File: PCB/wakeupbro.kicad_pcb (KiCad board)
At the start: 2 copper layers, 88.3 x 48.4 mm, 14 parts, among them J1 Conn_01x08_Pin, SW1 SW_Push, SW2 SW_Push, SW3 SW_Push, U1 XIAO-ESP32-C3-SMD

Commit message: Add finished PCB and exported step file of the PCB
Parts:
- added G***: LOGO, LOGO, F.Cu at (110.5, 49.6)
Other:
- board size 88.3 x 48.4 mm -> 90 x 50 mm

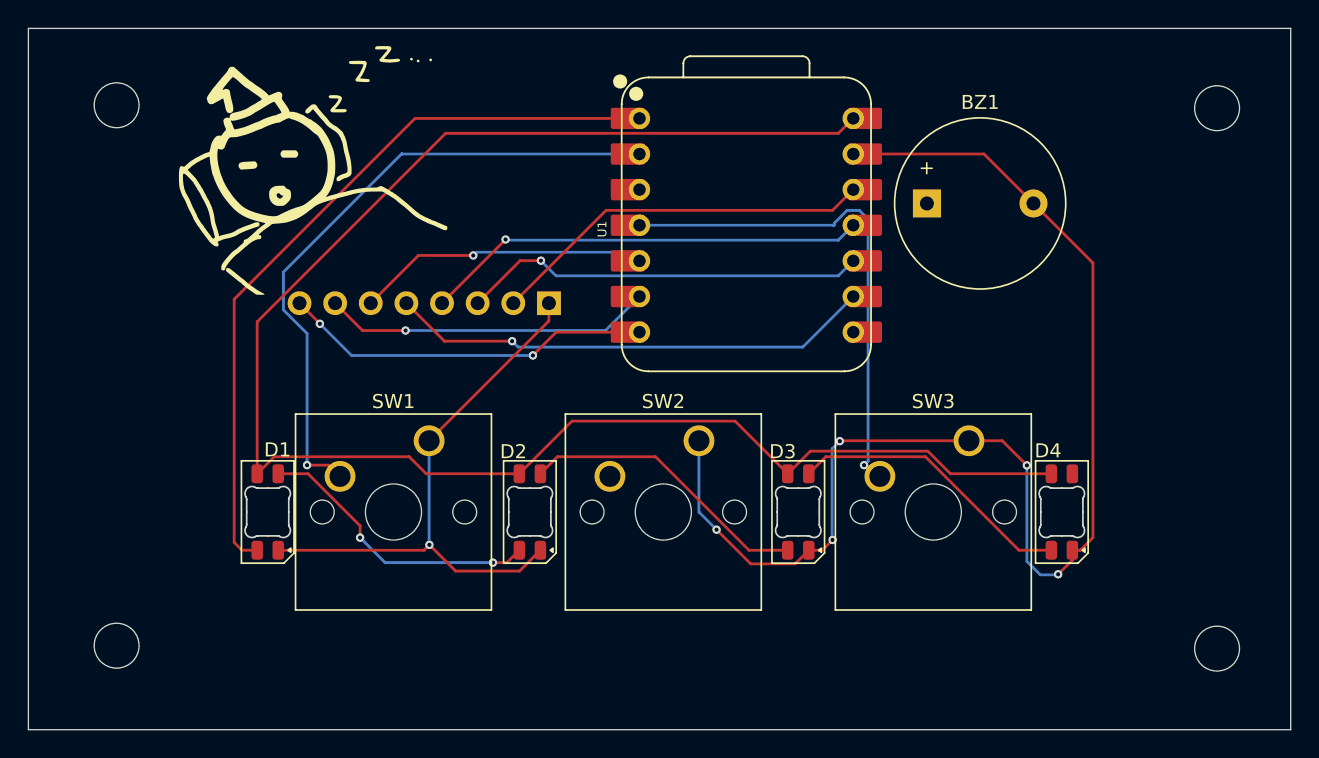
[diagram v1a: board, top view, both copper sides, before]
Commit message: Update PCB files. Going to start workig on firmware
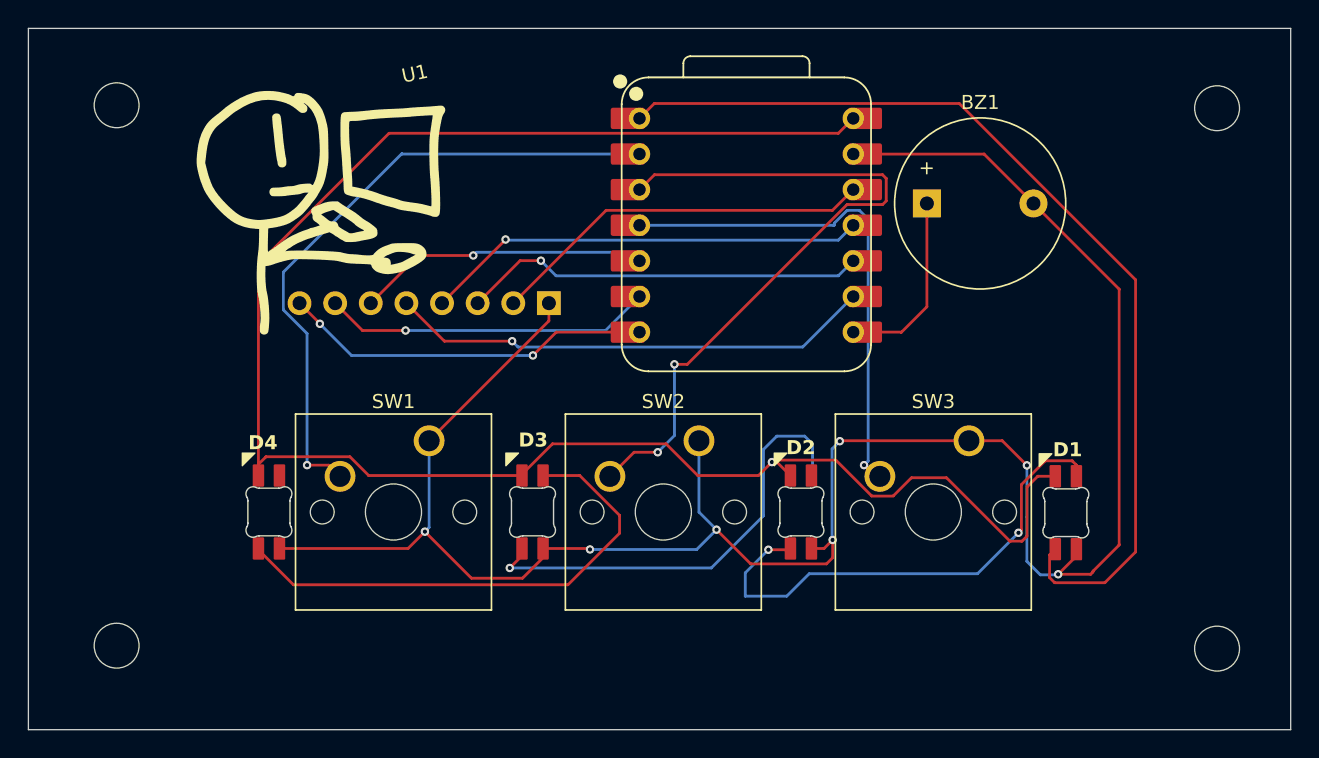
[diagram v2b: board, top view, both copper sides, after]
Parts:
- D1, D2, D3, D4: footprint LED_SMD:LED_SK6812MINI-E_3.2x2.8mm_P1.5mm_ReverseMount -> footprints:SK6812MINI-E_fixed; moved to B.Cu
- moved D1 56.8 mm to (164.3, 74.0)
- moved D4 56.6 mm to (107.5, 74.0)
- moved D2 19.2 mm to (145.4, 74.0)
- moved D3 19.0 mm to (126.3, 74.0)
- moved G*** 2.71 mm to (111.8, 52.0)
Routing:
- net SW2: track 0.00 -> 50.6 mm, vias 0 -> 2
- net GND: track 131.8 -> 153.0 mm, vias 6 -> 7
- net DIN: track 52.6 -> 69.8 mm
- net Net-(D3-DOUT): track 20.6 -> 36.3 mm
- net Net-(D1-DOUT): track 20.7 -> 36.0 mm
- net Net-(BZ1-+): track 0.00 -> 12.5 mm
- net Net-(D2-DOUT): track 20.9 -> 32.5 mm, vias 0 -> 1
- net +5V: track 121.4 -> 131.7 mm, vias 0 -> 1

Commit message: add final files
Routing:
- net Net-(D2-DOUT): track 32.5 -> 32.6 mm, vias 1 -> 2
